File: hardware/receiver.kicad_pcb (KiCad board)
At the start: 2 copper layers, 100 x 100 mm, 1 part, among them U1 ESP32-WROOM-32

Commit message: Worked on schematics and added some parts
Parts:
- added C1: 10u, Capacitor_SMD:C_1206_3216Metric, F.Cu at (124.5, 73.2)
- added C10: 10u, Capacitor_SMD:C_1206_3216Metric, F.Cu at (104.8, 94.4)
- added C11: 10u, Capacitor_SMD:C_1206_3216Metric, F.Cu at (114.6, 78.1)
- added C12: 100n, Capacitor_SMD:C_0402_1005Metric, F.Cu at (121.8, 80.7)
- added C13: 2.2u, Capacitor_SMD:C_0402_1005Metric, F.Cu at (96.4, 101.7)
- added C14: 2.2u, Capacitor_SMD:C_0402_1005Metric, F.Cu at (99.3, 101.7)
- added C15: 10u, Capacitor_SMD:C_1206_3216Metric, F.Cu at (124.5, 69.8)
- added C16: 100n, Capacitor_SMD:C_0402_1005Metric, F.Cu at (118.9, 82.7)
- added C17: 2.2n, Capacitor_SMD:C_0805_2012Metric, F.Cu at (112.9, 86.1)
- added C18: 2.2n, Capacitor_SMD:C_0805_2012Metric, F.Cu at (129.5, 69.6)
- added C2: 10u, Capacitor_SMD:C_1206_3216Metric, F.Cu at (120.3, 78.1)
- added C3: 10u, Capacitor_SMD:C_1206_3216Metric, F.Cu at (114.6, 81.4)
- added C4: 10u, Capacitor_SMD:C_1206_3216Metric, F.Cu at (86.5, 102.4)
- added C5: 10u, Capacitor_SMD:C_1206_3216Metric, F.Cu at (80.9, 102.4)
- added C6: 10u, Capacitor_SMD:C_1206_3216Metric, F.Cu at (92.2, 102.4)
- added C7: 100n, Capacitor_SMD:C_0402_1005Metric, F.Cu at (96.4, 103.6)
- added C8: 10u, Capacitor_SMD:C_1206_3216Metric, F.Cu at (75.2, 102.4)
- added C9: 100n, Capacitor_SMD:C_0402_1005Metric, F.Cu at (109.0, 93.7)
- added J1: USB-C, 31-M-12:HRO_TYPE-C-31-M-12, F.Cu at (51.3, 104.1)
- added J2: Left, RCJ-013:CUI_RCJ-013, F.Cu at (50.7, 120.6)
- added J3: Right, RCJ-013:CUI_RCJ-013, F.Cu at (50.5, 136.1)
- added R1: 470, Resistor_SMD:R_0402_1005Metric, F.Cu at (118.9, 80.7)
- added R2: 470, Resistor_SMD:R_0402_1005Metric, F.Cu at (103.4, 97.0)
- added U2: AMS1117-3.3, Package_TO_SOT_SMD:SOT-223-3_TabPin2, F.Cu at (116.7, 72.3)
- added U3: AMS1117-3.3, Package_TO_SOT_SMD:SOT-223-3_TabPin2, F.Cu at (106.9, 80.5)
- added U4: ESP32-WROOM-32E, RF_Module:ESP32-WROOM-32, F.Cu at (87.2, 89.7)
- added U5: PCM5102A, Package_SO:TSSOP-20_4.4x6.5mm_P0.65mm, F.Cu at (106.3, 88.7)
- U1: value ESP32-WROOM-32 -> AMS1117-3.3; footprint RF_Module:ESP32-WROOM-32 -> Package_TO_SOT_SMD:SOT-223-3_TabPin2
- moved U1 31.7 mm to (106.9, 72.3)
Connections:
- U1 pad 1: Net-(U1-Pad1) -> GND
- U1 pad 2: unconnected-(U1-Pad2) -> +3V3
- U1 pad 3: unconnected-(U1-Pad3) -> +5V

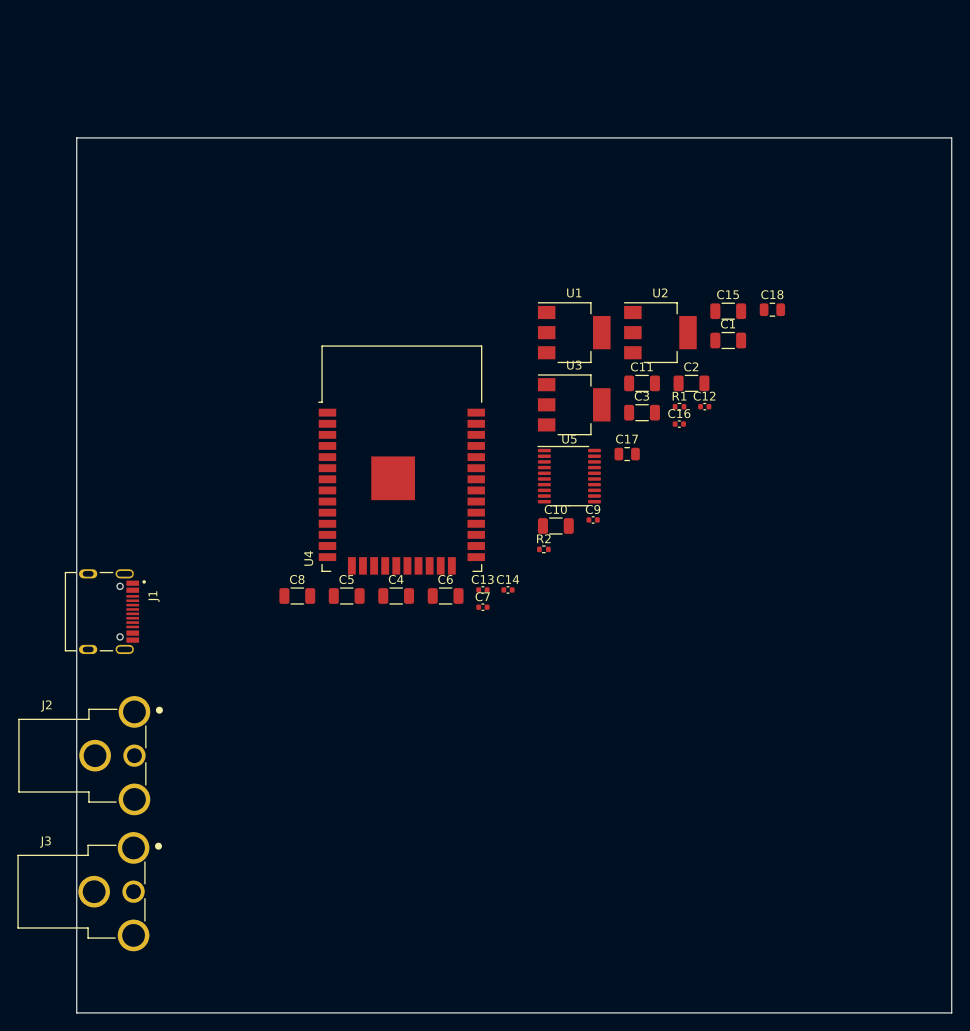
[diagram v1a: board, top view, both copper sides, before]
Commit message: Worked on schematic and split parts into seperate schematics
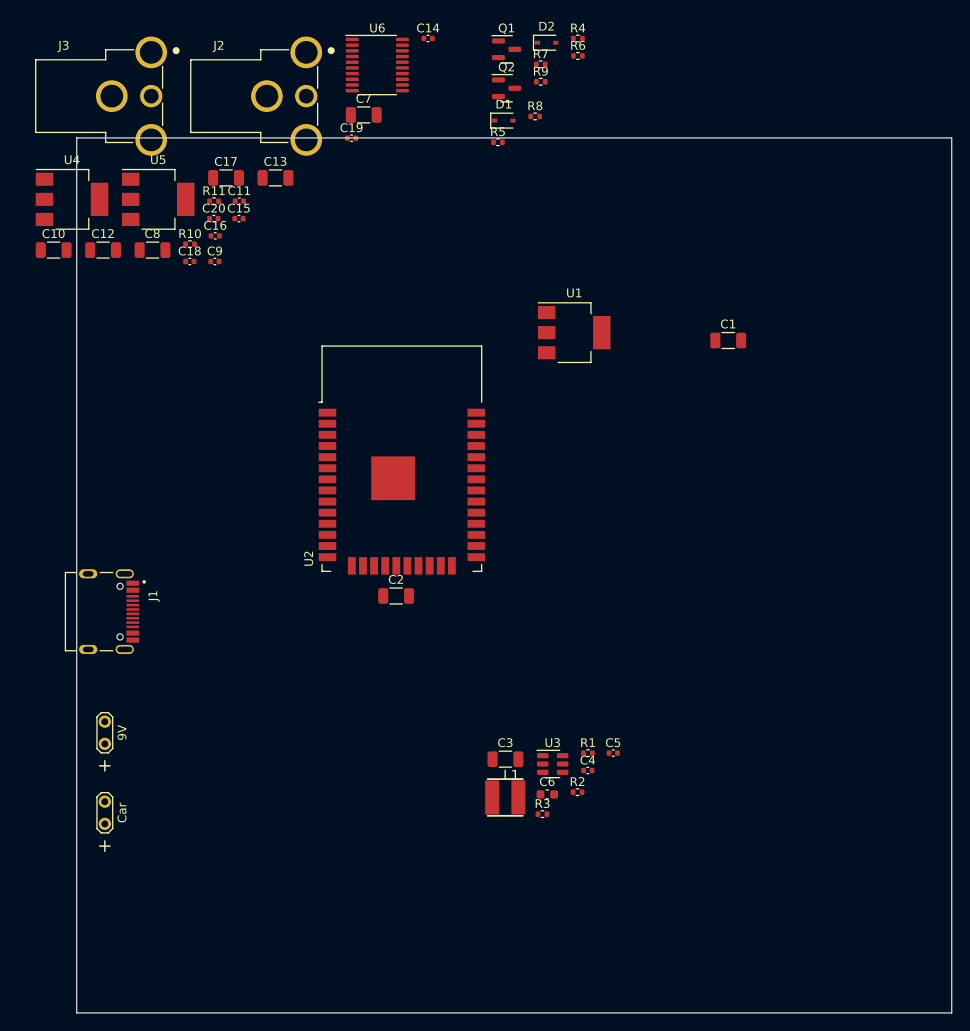
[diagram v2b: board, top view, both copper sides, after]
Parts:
- removed the C2 at (120.3, 78.1)
- removed the U2 at (116.7, 72.3)
- added BT1: 9V, TestPoint:TestPoint_2Pads_Pitch2.54mm_Drill0.8mm, F.Cu at (53.2, 119.3)
- added BT2: Car, TestPoint:TestPoint_2Pads_Pitch2.54mm_Drill0.8mm, F.Cu at (53.2, 128.4)
- added C19: 2.2n, Capacitor_SMD:C_0402_1005Metric, F.Cu at (81.4, 50.0)
- added C20: 2.2n, Capacitor_SMD:C_0402_1005Metric, F.Cu at (65.7, 59.2)
- added C4: 100n, Capacitor_SMD:C_0402_1005Metric, F.Cu at (108.4, 122.3)
- added D1: 1N5819WS, Diode_SMD:D_SOD-323, F.Cu at (98.8, 48.0)
- added D2: 1N5819WS, Diode_SMD:D_SOD-323, F.Cu at (103.7, 39.1)
- added L1: 75u, custom:IND-SMD_L4.0-W4.0_FNR40XXS, F.Cu at (99.0, 125.4)
- added Q1: AO3400A, Package_TO_SOT_SMD:SOT-23, F.Cu at (99.1, 39.9)
- added Q2: AO3401A, Package_TO_SOT_SMD:SOT-23, F.Cu at (99.1, 44.3)
- added R10: 470, Resistor_SMD:R_0402_1005Metric, F.Cu at (62.9, 62.1)
- added R11: 470, Resistor_SMD:R_0402_1005Metric, F.Cu at (65.7, 57.2)
- added R3: 120k, Resistor_SMD:R_0402_1005Metric, F.Cu at (103.2, 127.3)
- added R4: 100k, Resistor_SMD:R_0402_1005Metric, F.Cu at (107.3, 38.6)
- added R5: 100k, Resistor_SMD:R_0402_1005Metric, F.Cu at (98.1, 50.5)
- added R6: 20k, Resistor_SMD:R_0402_1005Metric, F.Cu at (107.3, 40.6)
- added R7: 10k, Resistor_SMD:R_0402_1005Metric, F.Cu at (103.0, 41.6)
- added R8: 68k, Resistor_SMD:R_0402_1005Metric, F.Cu at (102.4, 47.5)
- added R9: 20k, Resistor_SMD:R_0402_1005Metric, F.Cu at (103.0, 43.6)
- added U4: AMS1117-3.3, Package_TO_SOT_SMD:SOT-223-3_TabPin2, F.Cu at (49.5, 57.0)
- added U6: PCM5102A, Package_SO:TSSOP-20_4.4x6.5mm_P0.65mm, F.Cu at (84.4, 41.7)
- C11, C5: value 10u -> 100n; footprint Capacitor_SMD:C_1206_3216Metric -> Capacitor_SMD:C_0402_1005Metric
- C12, C7: value 100n -> 10u; footprint Capacitor_SMD:C_0402_1005Metric -> Capacitor_SMD:C_1206_3216Metric
- C13: value 2.2u -> 10u; footprint Capacitor_SMD:C_0402_1005Metric -> Capacitor_SMD:C_1206_3216Metric
- C14: value 2.2u -> 100n
- C15: value 10u -> 2.2u; footprint Capacitor_SMD:C_1206_3216Metric -> Capacitor_SMD:C_0402_1005Metric
- C16: value 100n -> 2.2u
- C17: value 2.2n -> 10u; footprint Capacitor_SMD:C_0805_2012Metric -> Capacitor_SMD:C_1206_3216Metric
- C18: value 2.2n -> 100n; footprint Capacitor_SMD:C_0805_2012Metric -> Capacitor_SMD:C_0402_1005Metric
- C3: value 10u -> 22u
- C6: value 10u -> 22uF; footprint Capacitor_SMD:C_1206_3216Metric -> Capacitor_SMD:C_0603_1608Metric
- R1: value 470 -> 100k
- R2: value 470 -> 24k
- U3: value AMS1117-3.3 -> TP6841S6-A; footprint Package_TO_SOT_SMD:SOT-223-3_TabPin2 -> Package_TO_SOT_SMD:SOT-23-6
- U5: value PCM5102A -> AMS1117-3.3; footprint Package_SO:TSSOP-20_4.4x6.5mm_P0.65mm -> Package_TO_SOT_SMD:SOT-223-3_TabPin2
- moved J3 90.9 mm to (52.6, 45.2)
- moved J2 77.9 mm to (70.3, 45.2)
- moved C12 71.1 mm to (53.0, 62.8)
- moved C18 66.8 mm to (62.9, 64.1)
- moved C10 65.5 mm to (47.4, 62.8)
- moved C14 63.7 mm to (90.2, 38.6)
- moved C7 57.9 mm to (82.8, 47.4)
- moved C16 57.2 mm to (65.8, 61.2)
- moved C15 56.9 mm to (68.5, 59.2)
- moved U5 56.6 mm to (59.3, 57.0)
- moved C17 55.7 mm to (67.1, 54.6)
- moved C13 52.7 mm to (72.7, 54.6)
- moved C9 52.4 mm to (65.8, 64.1)
- moved C11 50.5 mm to (68.6, 57.2)
- moved C8 42.9 mm to (58.7, 62.8)
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- renumbered C4 to C2, U4 to U2
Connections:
- C10 pad 1: +3V3 -> /Audio/CPVDD
- C10 pad 2: GND -> GNDA
- C11 pad 1: +3.3VA -> +3V3
- C11 pad 2: GNDA -> GND
- C12 pad 1: GNDA -> +3V3
- C12 pad 2: +3.3VA -> GND
- C13 pad 1: GNDA -> /Audio/AVDD
- C13 pad 2: Net-(C13-Pad2) -> GNDA
- C14 pad 2: Net-(C14-Pad2) -> /Audio/AVDD
- C15 pad 1: Net-(C15-Pad1) -> GNDA
- C15 pad 2: GND -> Net-(C15-Pad2)
- C16 pad 1: GND -> GNDA
- C16 pad 2: Net-(C15-Pad1) -> Net-(C16-Pad2)
- C17 pad 1: GNDA -> Net-(C17-Pad1)
- C17 pad 2: Net-(C17-Pad2) -> GND
- C18 pad 1: GNDA -> GND
- C18 pad 2: Net-(C18-Pad2) -> Net-(C17-Pad1)
- C3 pad 1: +5V -> Vin
- C5 pad 1: +3.3VA -> Net-(C5-Pad1)
- C5 pad 2: GND -> Net-(C5-Pad2)
- C6 pad 1: +3.3VP -> +5V
- C7 pad 1: GNDA -> +5V
- C7 pad 2: +3.3VP -> GND
- C8 pad 1: +3.3VP -> +5V
- C8 pad 2: GNDA -> GND
- C9 pad 1: +3V3 -> GNDA
- C9 pad 2: GND -> /Audio/CPVDD
- J2 pad 2: OUT_L -> /Audio/OUT_R
- J3 pad 2: OUT_R -> /Audio/OUT_R
- R1 pad 1: Net-(C17-Pad2) -> Vin
- R1 pad 2: OUT_L -> Net-(R1-Pad2)
- R2 pad 1: Net-(C18-Pad2) -> Net-(R2-Pad1)
- R2 pad 2: OUT_R -> GND
- U3 pad 1: GND -> Net-(C5-Pad1)
- U3 pad 2: +3.3VP -> GND
- U3 pad 3: +5V -> Net-(R2-Pad1)
- U5 pad 1: +3.3VP -> GND
- U5 pad 2: GNDA -> /Audio/CPVDD
- U5 pad 3: GNDA -> +5V
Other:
- board text added: "+"

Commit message: Finished first iteration of the PCB
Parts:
- removed BT1: 9V, TestPoint:TestPoint_2Pads_Pitch2.54mm_Drill0.8mm
- removed BT2: Car, TestPoint:TestPoint_2Pads_Pitch2.54mm_Drill0.8mm
- removed the J2 at (70.3, 45.2)
- added C1: 100n, Capacitor_SMD:C_0402_1005Metric, F.Cu at (111.1, 122.9)
- added C10: 22u, Capacitor_SMD:C_1206_3216Metric, F.Cu at (70.4, 125.6)
- added C11: 470u, Capacitor_THT:CP_Radial_D5.0mm_P2.50mm, F.Cu at (92.7, 144.5)
- added C26: 100n, Capacitor_SMD:C_0402_1005Metric, F.Cu at (55.6, 117.3)
- added C27: 100n, Capacitor_SMD:C_0402_1005Metric, F.Cu at (105.9, 128.0)
- added C28: 100n, Capacitor_SMD:C_0402_1005Metric, F.Cu at (74.1, 113.5)
- added C4: 100n, Capacitor_SMD:C_0402_1005Metric, F.Cu at (71.4, 114.6)
- added C5: 100n, Capacitor_SMD:C_0402_1005Metric, F.Cu at (62.2, 114.6)
- added D1: Green, LED_SMD:LED_0603_1608Metric, F.Cu at (67.8, 117.3)
- added D3: 1N5819WS, Diode_SMD:D_SOD-323, F.Cu at (64.2, 127.6)
- added J1: Conn_01x05_Male, Connector_JST:JST_XH_S5B-XH-A-1_1x05_P2.50mm_Horizontal, F.Cu at (56.8, 127.6)
- added J4: Right, RCJ-013:CUI_RCJ-013, F.Cu at (121.7, 138.2)
- added Q1: S8050, Package_TO_SOT_SMD:SOT-23, F.Cu at (100.7, 132.1)
- added Q2: S8050, Package_TO_SOT_SMD:SOT-23, F.Cu at (104.3, 132.1)
- added R1: 5.1k, Resistor_SMD:R_0402_1005Metric, F.Cu at (108.2, 116.0)
- added R10: 10k, Resistor_SMD:R_0402_1005Metric, F.Cu at (102.5, 129.5)
- added R11: 10k, Resistor_SMD:R_0402_1005Metric, F.Cu at (72.5, 114.6)
- added R12: 10k, Resistor_SMD:R_0402_1005Metric, F.Cu at (63.4, 114.6)
- added R16: 1k, Resistor_SMD:R_0402_1005Metric, F.Cu at (66.9, 127.6)
- added R2: 10k, Resistor_SMD:R_0402_1005Metric, F.Cu at (60.7, 123.6)
- added R3: 1M, Resistor_SMD:R_0402_1005Metric, F.Cu at (100.5, 110.5)
- added R4: 5.1k, Resistor_SMD:R_0402_1005Metric, F.Cu at (104.3, 116.0)
- added R5: 1k, Resistor_SMD:R_0402_1005Metric, F.Cu at (101.2, 119.6)
- added R8: 10k, Resistor_SMD:R_0402_1005Metric, F.Cu at (102.5, 128.5)
- added R9: 1k, Resistor_SMD:R_0402_1005Metric, F.Cu at (60.8, 117.9)
- added SW1: Enable, Button_Switch_SMD:SW_SPST_SKQG_WithStem, F.Cu at (67.8, 112.0)
- added SW2: Boot, Button_Switch_SMD:SW_SPST_SKQG_WithStem, F.Cu at (58.7, 112.0)
- added TP1: GND, TestPoint:TestPoint_Pad_D1.0mm, B.Cu at (61.2, 137.6)
- added TP10: OUT_R, TestPoint:TestPoint_Pad_D1.0mm, B.Cu at (109.5, 136.0)
- added TP11: GND, TestPoint:TestPoint_Pad_D1.0mm, B.Cu at (109.5, 138.6)
- added TP12: CAN_H, TestPoint:TestPoint_Pad_D1.0mm, B.Cu at (61.2, 130.1)
- added TP13: CAN_L, TestPoint:TestPoint_Pad_D1.0mm, B.Cu at (61.2, 132.6)
- added TP14: RX, TestPoint:TestPoint_Pad_D1.0mm, B.Cu at (99.2, 118.6)
- added TP15: TX, TestPoint:TestPoint_Pad_D1.0mm, B.Cu at (99.2, 116.1)
- added TP16: DTR, TestPoint:TestPoint_Pad_D1.0mm, B.Cu at (99.2, 121.2)
- added TP17: RTS, TestPoint:TestPoint_Pad_D1.0mm, B.Cu at (99.2, 123.8)
- added TP18: 5V, TestPoint:TestPoint_Pad_D1.0mm, B.Cu at (99.2, 113.5)
- added TP19: GND, TestPoint:TestPoint_Pad_D1.0mm, B.Cu at (99.2, 126.2)
- added TP2: 3V3, TestPoint:TestPoint_Pad_D1.0mm, B.Cu at (83.3, 133.6)
- added TP20: AVDD, TestPoint:TestPoint_Pad_D1.0mm, B.Cu at (111.0, 146.8)
- added TP21: CPVDD, TestPoint:TestPoint_Pad_D1.0mm, B.Cu at (83.1, 141.5)
- added TP3: 5V, TestPoint:TestPoint_Pad_D1.0mm, B.Cu at (77.1, 141.4)
- added TP4: V_in, TestPoint:TestPoint_Pad_D1.0mm, B.Cu at (70.6, 127.8)
- added TP5: CAR, TestPoint:TestPoint_Pad_D1.0mm, B.Cu at (61.2, 135.1)
- added TP6: DASH, TestPoint:TestPoint_Pad_D1.0mm, B.Cu at (61.2, 127.6)
- added TP7: SENSE, TestPoint:TestPoint_Pad_D1.0mm, B.Cu at (64.8, 124.2)
- added TP8: GND, TestPoint:TestPoint_Pad_D1.0mm, B.Cu at (109.5, 121.4)
- added TP9: OUT_L, TestPoint:TestPoint_Pad_D1.0mm, B.Cu at (109.5, 118.9)
- added U1: SN65HVD230, Package_SO:SOIC-8_3.9x4.9mm_P1.27mm, F.Cu at (56.4, 121.2)
- added U2: CH340C, Package_SO:SOIC-16_3.9x9.9mm_P1.27mm, F.Cu at (106.3, 122.3)
- D2: value 1N5819WS -> Blue; footprint Diode_SMD:D_SOD-323 -> LED_SMD:LED_0603_1608Metric
- J3: value Right -> Left
- R6: value 20k -> 1k
- R7: value 10k -> 1k
- moved U6 104.1 mm to (107.7, 143.3)
- moved C19 103.5 mm to (102.2, 141.4), turned to 180 degrees
- moved J3 102.6 mm to (121.7, 121.0), turned to 180 degrees
- moved C12 100.0 mm to (100.8, 145.8), turned to 180 degrees
- moved U8 97.3 mm to (97.0, 138.1), turned to 90 degrees
- moved Q3 93.4 mm to (69.9, 128.6)
- moved C18 93.1 mm to (100.8, 143.3), turned to 180 degrees
- moved Q4 93.0 mm to (67.6, 131.8)
- moved R17 92.8 mm to (70.4, 123.8)
- moved U7 92.4 mm to (85.4, 145.7), turned to 180 degrees
- moved D4 92.0 mm to (63.0, 132.7), turned to 180 degrees
- moved R20 91.3 mm to (62.0, 125.1), turned to 90 degrees
- moved D2 90.3 mm to (58.7, 117.3)
- moved C25 90.0 mm to (112.1, 136.3), turned to -90 degrees
- moved R22 89.9 mm to (103.1, 138.9)
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- renumbered C7 to C12, C8 to C13, C9 to C14, C10 to C15, C11 to C16, C12 to C17, C13 to C18, C14 to C19, C1 to C2, C15 to C20, C16 to C21, C17 to C22, C18 to C23, C19 to C24, C20 to C25, C2 to C3, C3 to C6, C4 to C7, C5 to C8, C6 to C9, D1 to D4, J1 to J2, Q1 to Q3, Q2 to Q4, R1 to R13, R2 to R14, R3 to R15, R4 to R17, R5 to R18, R8 to R19, R9 to R20, R10 to R21, R11 to R22, U1 to U3, U2 to U4, U3 to U5, U4 to U6, U5 to U7, U6 to U8
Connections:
- net POWER_CONTROL renamed Net-(C10-Pad1)
- C14 pad 1: GNDA -> GND
- C15 pad 2: GNDA -> GND
- C18 pad 2: GNDA -> GND
- C19 pad 1: GNDA -> GND
- C20 pad 1: GNDA -> GND
- C21 pad 1: GNDA -> GND
- C24 pad 1: GNDA -> GND
- C24 pad 2: Net-(C19-Pad2) -> /OUT_L
- C25 pad 1: GNDA -> GND
- C25 pad 2: Net-(C20-Pad2) (its old number) -> /OUT_R
- C6 pad 1: Vin -> /V_in
- C7 pad 2: Vin -> /V_in
- D2 pad 1: Vin -> GND
- D2 pad 2: +12V -> Net-(D2-Pad2)
- D4 pad 1: Net-(D1-Pad1) -> Net-(D4-Pad1)
- D4 pad 2: +BATT -> /CAR
- J2 pad A1B12: Net-(J1-PadA1B12) -> GND
- J2 pad A4B9: Net-(J1-PadA4B9) -> +5V
- J2 pad A5: unconnected-(J1-PadA5) -> Net-(J2-PadA5)
- J2 pad A6: unconnected-(J1-PadA6) -> /D+
- J2 pad A7: unconnected-(J1-PadA7) -> /D-
- J2 pad B1A12: Net-(J1-PadA1B12) -> GND
- J2 pad B4A9: Net-(J1-PadA4B9) -> +5V
- J2 pad B5: unconnected-(J1-PadB5) -> Net-(J2-PadB5)
- J2 pad B6: unconnected-(J1-PadB6) -> /D+
- J2 pad B7: unconnected-(J1-PadB7) -> /D-
- J3 pad 1A: GNDA -> GND
- J3 pad 1B: GNDA -> GND
- J3 pad 1C: GNDA -> GND
- J3 pad 2: /Audio/OUT_R -> /OUT_L
- Q4 pad 2: Vin -> Net-(D4-Pad1)
- Q4 pad 3: Net-(D1-Pad1) -> /V_in
- R13 pad 1: Vin -> /V_in
- R18 pad 1: Net-(D1-Pad1) -> Net-(D4-Pad1)
- R19 pad 1: +12V -> /DASH
- R19 pad 2: SUPPLY_SENSE -> /Sense
- R20 pad 1: SUPPLY_SENSE -> /Sense
- R21 pad 1: Net-(C19-Pad2) -> /OUT_L
- R21 pad 2: /Audio/OUT_L -> Net-(R21-Pad2)
- R22 pad 1: Net-(C20-Pad2) (its old number) -> Net-(R22-Pad1)
- R22 pad 2: /Audio/OUT_R -> /OUT_R
- R6 pad 1: +BATT -> /TX
- R6 pad 2: BATTERY_SENSE -> Net-(R6-Pad2)
- R7 pad 1: BATTERY_SENSE -> +3V3
- R7 pad 2: GND -> Net-(D1-Pad2)
- U4 pad 1: Net-(U2-Pad1) -> GND
- U4 pad 10: unconnected-(U2-Pad10) -> /Sense
- U4 pad 15: Net-(U2-Pad1) -> GND
- U4 pad 2: unconnected-(U2-Pad2) -> +3V3
- U4 pad 25: unconnected-(U2-Pad25) -> /BOOT
- U4 pad 26: unconnected-(U2-Pad26) -> /MUTE
- U4 pad 27: unconnected-(U2-Pad27) -> /WS
- U4 pad 28: unconnected-(U2-Pad28) -> /DATA
- U4 pad 29: unconnected-(U2-Pad29) -> /BCK
- U4 pad 3: unconnected-(U2-Pad3) -> /EN
- U4 pad 34: unconnected-(U2-Pad34) -> /RX
- U4 pad 35: unconnected-(U2-Pad35) -> /TX
- U4 pad 38: Net-(U2-Pad1) -> GND
- U4 pad 39: Net-(U2-Pad1) -> GND
- U4 pad 6: unconnected-(U2-Pad6) -> /BLUE
- U4 pad 7: unconnected-(U2-Pad7) -> /CRX
- U4 pad 8: unconnected-(U2-Pad8) -> /CTX
- U4 pad 9: unconnected-(U2-Pad9) -> /MODE
- U5 pad 5: Vin -> /V_in
- U6 pad 2: /Audio/AVVD -> /Audio/AVDD
- U8 pad 13: BCK -> /BCK
- U8 pad 14: DATA -> /DATA
- U8 pad 15: WS -> /WS
- U8 pad 17: unconnected-(U6-Pad17) -> /MUTE
- U8 pad 2: GNDA -> GND
- U8 pad 3: GNDA -> GND
- U8 pad 6: Net-(C19-Pad2) -> Net-(R21-Pad2)
- U8 pad 7: Net-(C20-Pad2) (its old number) -> Net-(R22-Pad1)
- U8 pad 9: GNDA -> GND
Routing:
- net +3V3: track 0.00 -> 120.4 mm, vias 0 -> 13
- net +5V: track 0.00 -> 110.1 mm, vias 0 -> 5
- net GND: track 0.00 -> 73.4 mm, vias 0 -> 163
- net /BOOT: track 0.00 -> 61.0 mm, vias 0 -> 3
- net /EN: track 0.00 -> 51.1 mm, vias 0 -> 2
- net /OUT_L: track 0.00 -> 33.4 mm
- net /CAN-: track 0.00 -> 21.3 mm
- net /CAN+: track 0.00 -> 21.2 mm
- net /OUT_R: track 0.00 -> 21.0 mm
- net /Sense: track 0.00 -> 19.8 mm, vias 0 -> 1
- net /CTX: track 0.00 -> 19.5 mm
- net /CRX: track 0.00 -> 19.0 mm
- net Net-(J2-PadS1): track 0.00 -> 18.4 mm
- net /MODE: track 0.00 -> 17.4 mm
- net /DTR: track 0.00 -> 16.9 mm, vias 0 -> 1
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- added copper zone on F.Cu, net +3V3
- added copper zone on F.Cu, net +5V
- added copper zone on F.Cu, net /Audio/AVDD
- added copper zone on F.Cu, net /Audio/CPVDD
- added copper zone on B.Cu, net GND
- added copper zone on F.Cu, net GND
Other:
- board size 100 x 100 mm -> 71.8 x 43.7 mm
- board text added: "Bluetooth Car Receiver (Rev.1) By: Tim Huizinga"
- board text removed: "+"
